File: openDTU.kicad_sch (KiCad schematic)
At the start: 3 parts, among them U1 ESP32NodeMCU, U2 NRF24L01+PA+LNA_Breakout

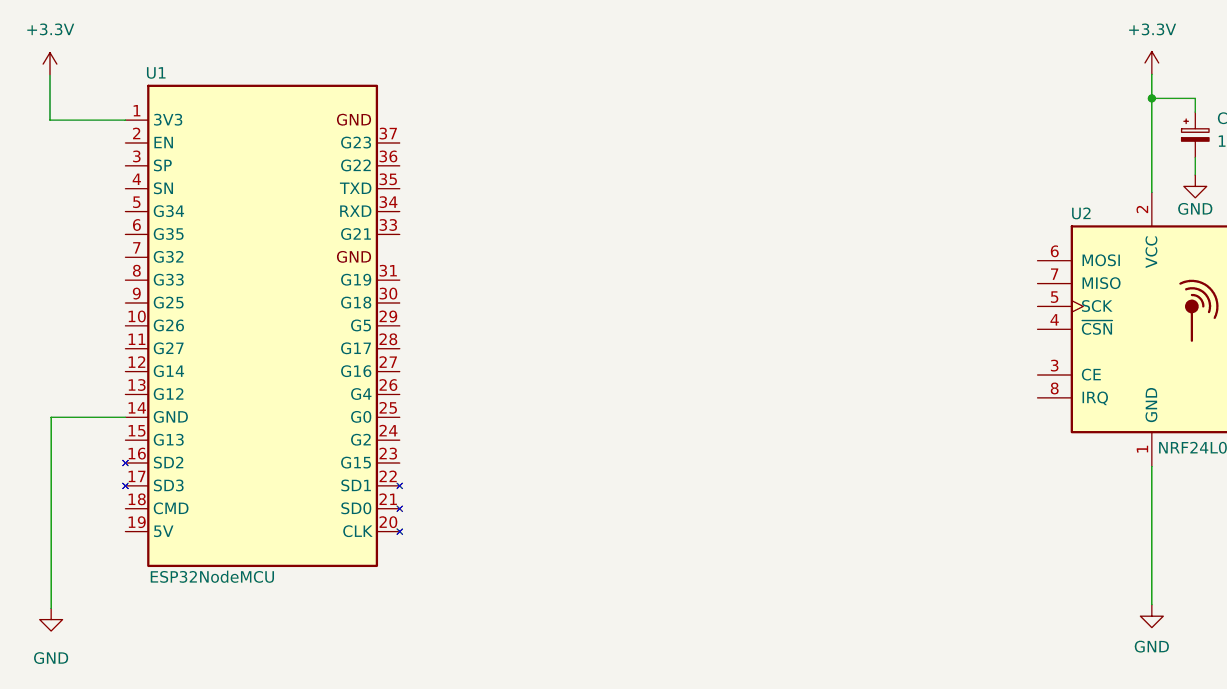
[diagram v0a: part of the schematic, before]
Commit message: connecting nRF24L01+ to the ESP32 in schematic
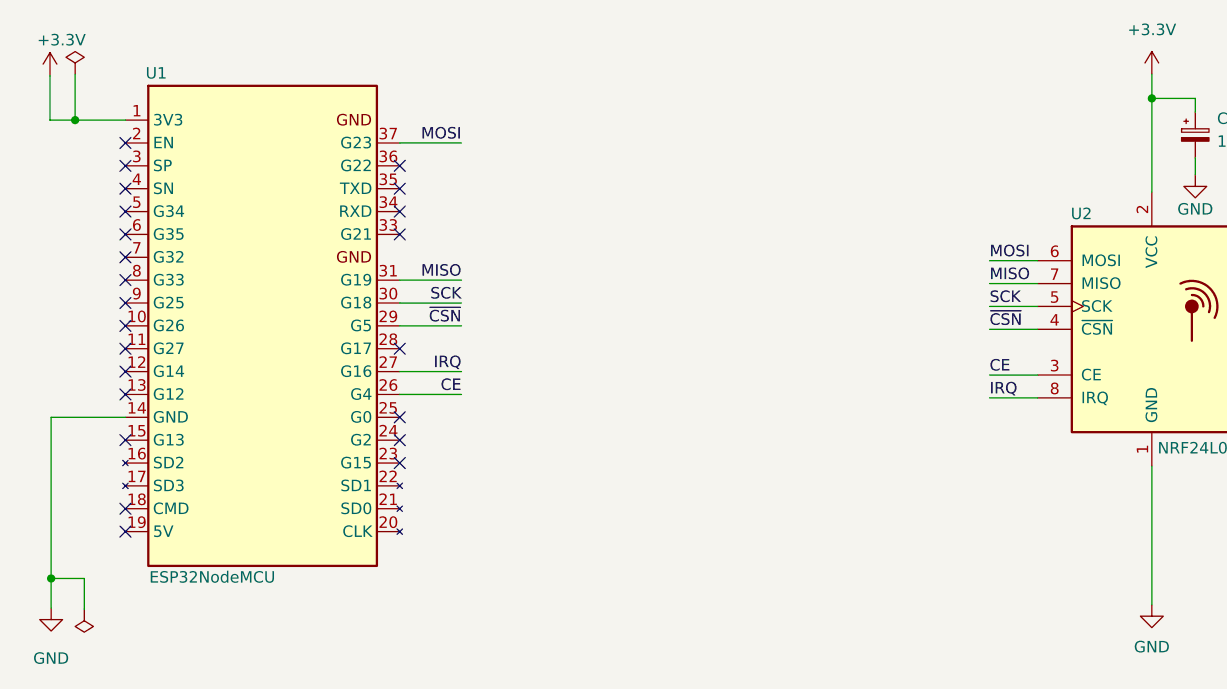
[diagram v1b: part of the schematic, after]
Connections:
- net CE: now reaches U1.26 (G4)
- net CE: now also U2.3 (CE)
- net IRQ: now reaches U1.27 (G16)
- net IRQ: now also U2.8 (IRQ)
- net ~{CSN}: now reaches U1.29 (G5)
- net ~{CSN}: now also U2.4 (~{CSN})
- net SCK: now reaches U1.30 (G18)
- net SCK: now also U2.5 (SCK)
- net MISO: now reaches U1.31 (G19)
- net MISO: now also U2.7 (MISO)
- net MOSI: now reaches U1.37 (G23)
- net MOSI: now also U2.6 (MOSI)
- no-connect marks 0 -> 23
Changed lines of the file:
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@@
 (kicad_sch (version 20211123) (generator eeschema)
   (paper "A4")
+  (junction (at 81.407 77.343) (diameter 0) (color 0 0 0 0)
+  )
   (junction (at 201.041 74.93) (diameter 0) (color 0 0 0 0)
   )
+  (junction (at 78.74 128.27) (diameter 0) (color 0 0 0 0)
+  )
+  (no_connect (at 86.995 123.063))
+  (no_connect (at 86.995 120.523))
+  (no_connect (at 86.995 107.823))
+  (no_connect (at 86.995 79.883))
+  (no_connect (at 86.995 92.583))
+  (no_connect (at 86.995 90.043))
+  (no_connect (at 86.995 87.503))
+  (no_connect (at 86.995 84.963))
+  (no_connect (at 86.995 82.423))
+  (no_connect (at 117.475 90.043))
+  (no_connect (at 117.475 84.963))
+  (no_connect (at 117.475 87.503))
+  (no_connect (at 117.475 82.423))
+  (no_connect (at 117.475 102.743))
+  (no_connect (at 117.475 110.363))
+  (no_connect (at 117.475 112.903))
+  (no_connect (at 117.475 115.443))
+  (no_connect (at 86.995 112.903))
+  (no_connect (at 86.995 105.283))
+  (no_connect (at 86.995 102.743))
+  (no_connect (at 86.995 100.203))
+  (no_connect (at 86.995 97.663))
+  (no_connect (at 86.995 95.123))
+  (wire (pts (xy 117.475 79.883) (xy 124.333 79.883))
+    (stroke (width 0) (type default) (color 0 0 0 0))
+  )
+  (wire (pts (xy 117.475 105.283) (xy 124.333 105.283))
+    (stroke (width 0) (type default) (color 0 0 0 0))
+  )
   (wire (pts (xy 205.867 74.93) (xy 201.041 74.93))
     (stroke (width 0) (type default) (color 0 0 0 0))
   )
+  (wire (pts (xy 183.007 100.584) (xy 188.341 100.584))
+    (stroke (width 0) (type default) (color 0 0 0 0))
+  )
+  (wire (pts (xy 117.475 97.663) (xy 124.333 97.663))
+    (stroke (width 0) (type default) (color 0 0 0 0))
+  )
   (wire (pts (xy 78.74 110.363) (xy 86.995 110.363))
     (stroke (width 0) (type default) (color 0 0 0 0))
   )
-  (wire (pts (xy 78.74 131.572) (xy 78.74 110.363))
+  (wire (pts (xy 78.74 131.572) (xy 78.74 128.27))
+    (stroke (width 0) (type default) (color 0 0 0 0))
+  )
+  (wire (pts (xy 117.475 95.123) (xy 124.333 95.123))
+    (stroke (width 0) (type default) (color 0 0 0 0))
+  )
+  (wire (pts (xy 78.74 128.27) (xy 78.74 110.363))
     (stroke (width 0) (type default) (color 0 0 0 0))
   )
@@
     (stroke (width 0) (type default) (color 0 0 0 0))
   )
+  (wire (pts (xy 183.007 98.044) (xy 188.341 98.044))
+    (stroke (width 0) (type default) (color 0 0 0 0))
+  )
+  (wire (pts (xy 117.475 107.823) (xy 124.333 107.823))
+    (stroke (width 0) (type default) (color 0 0 0 0))
+  )
+  (wire (pts (xy 183.007 108.204) (xy 188.341 108.204))
+    (stroke (width 0) (type default) (color 0 0 0 0))
+  )
   (wire (pts (xy 205.867 81.534) (xy 205.867 83.439))
     (stroke (width 0) (type default) (color 0 0 0 0))
@@
     (stroke (width 0) (type default) (color 0 0 0 0))
   )
+  (wire (pts (xy 183.007 95.504) (xy 188.341 95.504))
+    (stroke (width 0) (type default) (color 0 0 0 0))
+  )
+  (wire (pts (xy 183.007 105.664) (xy 188.341 105.664))
+    (stroke (width 0) (type default) (color 0 0 0 0))
+  )
+  (wire (pts (xy 117.475 100.203) (xy 124.333 100.203))
+    (stroke (width 0) (type default) (color 0 0 0 0))
+  )
+  (wire (pts (xy 81.407 77.343) (xy 86.995 77.343))
+    (stroke (width 0) (type default) (color 0 0 0 0))
+  )
   (wire (pts (xy 201.041 85.344) (xy 201.041 74.93))
     (stroke (width 0) (type default) (color 0 0 0 0))
   )
+  (wire (pts (xy 81.407 72.263) (xy 81.407 77.343))
+    (stroke (width 0) (type default) (color 0 0 0 0))
+  )
   (wire (pts (xy 201.041 74.93) (xy 201.041 72.263))
     (stroke (width 0) (type default) (color 0 0 0 0))
   )
-  (wire (pts (xy 78.613 77.343) (xy 86.995 77.343))
-    (stroke (width 0) (type default) (color 0 0 0 0))
+  (wire (pts (xy 82.423 128.27) (xy 78.74 128.27))
+    (stroke (width 0) (type default) (color 0 0 0 0))
+  )
+  (wire (pts (xy 183.007 92.964) (xy 188.341 92.964))
+    (stroke (width 0) (type default) (color 0 0 0 0))
+  )
+  (wire (pts (xy 78.613 77.343) (xy 81.407 77.343))
+    (stroke (width 0) (type default) (color 0 0 0 0))
+  )
+  (wire (pts (xy 82.423 131.699) (xy 82.423 128.27))
+    (stroke (width 0) (type default) (color 0 0 0 0))
+  )
+  (label "CE" (at 124.333 107.823 180)
+    (effects (font (size 1.27 1.27)) (justify right bottom))
+  )
+  (label "IRQ" (at 124.333 105.283 180)
+    (effects (font (size 1.27 1.27)) (justify right bottom))
+  )
+  (label "~{CSN}" (at 124.333 100.203 180)
+    (effects (font (size 1.27 1.27)) (justify right bottom))
+  )
+  (label "MISO" (at 124.333 95.123 180)
+    (effects (font (size 1.27 1.27)) (justify right bottom))
+  )
+  (label "SCK" (at 183.007 98.044 0)
+    (effects (font (size 1.27 1.27)) (justify left bottom))
+  )
+  (label "MOSI" (at 183.007 92.964 0)
+    (effects (font (size 1.27 1.27)) (justify left bottom))
+  )
+  (label "~{CSN}" (at 183.007 100.584 0)
+    (effects (font (size 1.27 1.27)) (justify left bottom))
+  )
+  (label "MOSI" (at 124.333 79.883 180)
+    (effects (font (size 1.27 1.27)) (justify right bottom))
+  )
+  (label "MISO" (at 183.007 95.504 0)
+    (effects (font (size 1.27 1.27)) (justify left bottom))
+  )
+  (label "CE" (at 183.007 105.664 0)
+    (effects (font (size 1.27 1.27)) (justify left bottom))
+  )
+  (label "IRQ" (at 183.007 108.204 0)
+    (effects (font (size 1.27 1.27)) (justify left bottom))
+  )
+  (label "SCK" (at 124.333 97.663 180)
+    (effects (font (size 1.27 1.27)) (justify right bottom))
   )
   (symbol (lib_id "ESP32-NodeMCU_WROOM_32:ESP32NodeMCU") (at 100.965 100.203 0) (unit 1)
@@
     (pin "2")
   )
+  (symbol (lib_id "power:PWR_FLAG") (at 81.407 72.263 0) (unit 1)
+    (in_bom yes) (on_board yes)
+    (property "Reference" "#FLG0101" (id 0) (at 81.407 70.358 0)
+      (effects (font (size 1.27 1.27)) hide)
+    )
+    (property "Value" "PWR_FLAG" (id 1) (at 81.407 67.31 0)
+      (effects (font (size 1.27 1.27)) hide)
+    )
+    (property "Footprint" "" (id 2) (at 81.407 72.263 0)
+      (effects (font (size 1.27 1.27)) hide)
+    )
+    (property "Datasheet" "~" (id 3) (at 81.407 72.263 0)
+      (effects (font (size 1.27 1.27)) hide)
+    )
+    (pin "1")
+  )
   (symbol (lib_id "nRF24L01+PA+LNA:NRF24L01+PA+LNA_Breakout") (at 201.041 100.584 0) (unit 1)
     (in_bom yes) (on_board yes)
@@
   )
   (symbol (lib_id "power:+3.3V") (at 78.613 72.39 0) (unit 1)
-    (in_bom yes) (on_board yes) (fields_autoplaced)
+    (in_bom yes) (on_board yes)
     (property "Reference" "#PWR01" (id 0) (at 78.613 76.2 0)
       (effects (font (size 1.27 1.27)) hide)
     )
-    (property "Value" "+3.3V" (id 1) (at 78.613 67.31 0))
+    (property "Value" "+3.3V" (id 1) (at 79.883 68.453 0))
     (property "Footprint" "" (id 2) (at 78.613 72.39 0)
       (effects (font (size 1.27 1.27)) hide)
@@
     (pin "1")
   )
+  (symbol (lib_id "power:PWR_FLAG") (at 82.423 131.699 180) (unit 1)
+    (in_bom yes) (on_board yes) (fields_autoplaced)
+    (property "Reference" "#FLG0102" (id 0) (at 82.423 133.604 0)
+      (effects (font (size 1.27 1.27)) hide)
+    )
+    (property "Value" "PWR_FLAG" (id 1) (at 82.423 137.16 0)
+      (effects (font (size 1.27 1.27)) hide)
+    )
+    (property "Footprint" "" (id 2) (at 82.423 131.699 0)
+      (effects (font (size 1.27 1.27)) hide)
+    )
+    (property "Datasheet" "~" (id 3) (at 82.423 131.699 0)
+      (effects (font (size 1.27 1.27)) hide)
+    )
+    (pin "1")
+  )
   (symbol (lib_id "power:GND") (at 205.867 83.439 0) (unit 1)
     (in_bom yes) (on_board yes)
@@
   )
   (symbol_instances
+    (path "/536b3283-000a-432e-99b7-ba775fb60222"
+      (reference "#FLG0101") (unit 1) (value "PWR_FLAG") (footprint "")
+    )
+    (path "/ef63471f-d6f9-4ef1-a573-5457f22963dc"
+      (reference "#FLG0102") (unit 1) (value "PWR_FLAG") (footprint "")
+    )
     (path "/cd7881ec-7c4b-4a13-beb3-1ca57ea56ce1"
       (reference "#PWR01") (unit 1) (value "+3.3V") (footprint "")

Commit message: adding OpenDTU Logo and some informations on the silkscreen
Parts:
- C1: footprint Capacitor_THT:CP_Radial_D6.3mm_P2.50mm -> Capacitor_THT:CP_Radial_D5.0mm_P2.50mm; Manf (none) -> https://www.reichelt.de/de/de/elko-radial-10-f-25-v-105-4-x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
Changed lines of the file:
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@@
       (effects (font (size 1.27 1.27)) (justify left))
     )
-    (property "Footprint" "Capacitor_THT:CP_Radial_D6.3mm_P2.50mm" (id 2) (at 205.867 78.994 0)
+    (property "Footprint" "Capacitor_THT:CP_Radial_D5.0mm_P2.50mm" (id 2) (at 205.867 78.994 0)
       (effects (font (size 1.27 1.27)) hide)
     )
     (property "Datasheet" "~" (id 3) (at 205.867 78.994 0)
+      (effects (font (size 1.27 1.27)) hide)
+    )
+    (property "Manf" "https://www.reichelt.de/de/de/elko-radial-10-f-25-v-105-4-x-7-mm-rm-2-5-ga-a-10u-25-3-p228366.html?r=1" (id 4) (at 205.867 78.994 0)
       (effects (font (size 1.27 1.27)) hide)
     )
@@
     )
     (path "/45a05041-9552-4705-9a03-84bdba86756f"
-      (reference "C1") (unit 1) (value "10uF") (footprint "Capacitor_THT:CP_Radial_D6.3mm_P2.50mm")
+      (reference "C1") (unit 1) (value "10uF") (footprint "Capacitor_THT:CP_Radial_D5.0mm_P2.50mm")
     )
     (path "/0626e94d-7e2b-4dab-a267-2ede4e5d9e77"

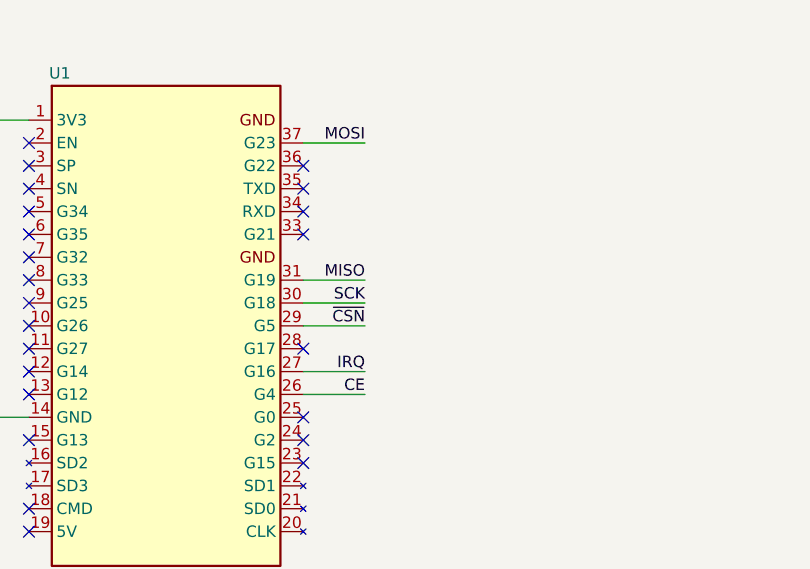
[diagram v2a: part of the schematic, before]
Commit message: Adding some Testpads for signals between ESP32 and nRF24L01+. Adding vias to connect Bottom and Top GND Copper Zone.
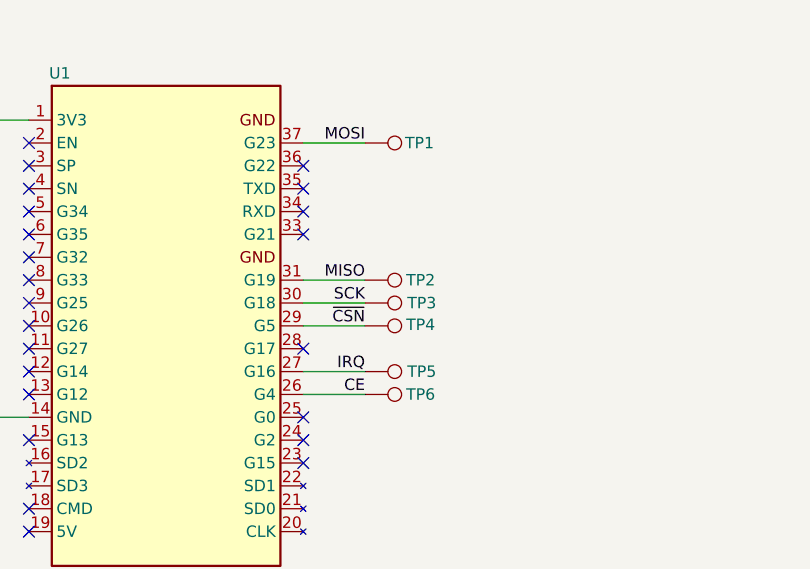
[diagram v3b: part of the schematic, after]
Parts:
- added TP1, TP2, TP3, TP4, TP5, TP6: TestPoint, TestPoint:TestPoint_THTPad_D1.5mm_Drill0.7mm, symbol Connector:TestPoint
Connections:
- net CE: now also TP6.1
- net IRQ: now also TP5.1
- net MISO: now also TP2.1
- net MOSI: now also TP1.1
- net SCK: now also TP3.1
- net ~{CSN}: now also TP4.1
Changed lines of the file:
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@@
     (pin "9")
+  )
+  (symbol (lib_id "Connector:TestPoint") (at 124.333 95.123 270) (unit 1)
+    (in_bom yes) (on_board yes)
+    (property "Reference" "TP2" (id 0) (at 128.905 95.123 90)
+      (effects (font (size 1.27 1.27)) (justify left))
+    )
+    (property "Value" "TestPoint" (id 1) (at 129.54 96.3929 90)
+      (effects (font (size 1.27 1.27)) (justify left) hide)
+    )
+    (property "Footprint" "TestPoint:TestPoint_THTPad_D1.5mm_Drill0.7mm" (id 2) (at 124.333 100.203 0)
+      (effects (font (size 1.27 1.27)) hide)
+    )
+    (property "Datasheet" "~" (id 3) (at 124.333 100.203 0)
+      (effects (font (size 1.27 1.27)) hide)
+    )
+    (pin "1")
   )
   (symbol (lib_id "power:GND") (at 201.041 131.191 0) (unit 1)
@@
     )
     (property "Datasheet" "~" (id 3) (at 81.407 72.263 0)
+      (effects (font (size 1.27 1.27)) hide)
+    )
+    (pin "1")
+  )
+  (symbol (lib_id "Connector:TestPoint") (at 124.333 107.823 270) (unit 1)
+    (in_bom yes) (on_board yes)
+    (property "Reference" "TP6" (id 0) (at 128.905 107.823 90)
+      (effects (font (size 1.27 1.27)) (justify left))
+    )
+    (property "Value" "TestPoint" (id 1) (at 129.54 109.0929 90)
+      (effects (font (size 1.27 1.27)) (justify left) hide)
+    )
+    (property "Footprint" "TestPoint:TestPoint_THTPad_D1.5mm_Drill0.7mm" (id 2) (at 124.333 112.903 0)
+      (effects (font (size 1.27 1.27)) hide)
+    )
+    (property "Datasheet" "~" (id 3) (at 124.333 112.903 0)
+      (effects (font (size 1.27 1.27)) hide)
+    )
+    (pin "1")
+  )
+  (symbol (lib_id "Connector:TestPoint") (at 124.333 97.663 270) (unit 1)
+    (in_bom yes) (on_board yes)
+    (property "Reference" "TP3" (id 0) (at 129.032 97.663 90)
+      (effects (font (size 1.27 1.27)) (justify left))
+    )
+    (property "Value" "TestPoint" (id 1) (at 129.54 98.9329 90)
+      (effects (font (size 1.27 1.27)) (justify left) hide)
+    )
+    (property "Footprint" "TestPoint:TestPoint_THTPad_D1.5mm_Drill0.7mm" (id 2) (at 124.333 102.743 0)
+      (effects (font (size 1.27 1.27)) hide)
+    )
+    (property "Datasheet" "~" (id 3) (at 124.333 102.743 0)
       (effects (font (size 1.27 1.27)) hide)
     )
@@
     (pin "8")
   )
+  (symbol (lib_id "Connector:TestPoint") (at 124.333 79.883 270) (unit 1)
+    (in_bom yes) (on_board yes)
+    (property "Reference" "TP1" (id 0) (at 128.778 79.883 90)
+      (effects (font (size 1.27 1.27)) (justify left))
+    )
+    (property "Value" "TestPoint" (id 1) (at 129.54 81.1529 90)
+      (effects (font (size 1.27 1.27)) (justify left) hide)
+    )
+    (property "Footprint" "TestPoint:TestPoint_THTPad_D1.5mm_Drill0.7mm" (id 2) (at 124.333 84.963 0)
+      (effects (font (size 1.27 1.27)) hide)
+    )
+    (property "Datasheet" "~" (id 3) (at 124.333 84.963 0)
+      (effects (font (size 1.27 1.27)) hide)
+    )
+    (pin "1")
+  )
   (symbol (lib_id "power:+3.3V") (at 78.613 72.39 0) (unit 1)
     (in_bom yes) (on_board yes)
@@
     )
     (property "Datasheet" "" (id 3) (at 201.041 72.263 0)
+      (effects (font (size 1.27 1.27)) hide)
+    )
+    (pin "1")
+  )
+  (symbol (lib_id "Connector:TestPoint") (at 124.333 105.283 270) (unit 1)
+    (in_bom yes) (on_board yes)
+    (property "Reference" "TP5" (id 0) (at 129.032 105.283 90)
+      (effects (font (size 1.27 1.27)) (justify left))
+    )
+    (property "Value" "TestPoint" (id 1) (at 129.54 106.5529 90)
+      (effects (font (size 1.27 1.27)) (justify left) hide)
+    )
+    (property "Footprint" "TestPoint:TestPoint_THTPad_D1.5mm_Drill0.7mm" (id 2) (at 124.333 110.363 0)
+      (effects (font (size 1.27 1.27)) hide)
+    )
+    (property "Datasheet" "~" (id 3) (at 124.333 110.363 0)
+      (effects (font (size 1.27 1.27)) hide)
+    )
+    (pin "1")
+  )
+  (symbol (lib_id "Connector:TestPoint") (at 124.333 100.203 270) (unit 1)
+    (in_bom yes) (on_board yes)
+    (property "Reference" "TP4" (id 0) (at 128.905 100.076 90)
+      (effects (font (size 1.27 1.27)) (justify left))
+    )
+    (property "Value" "TestPoint" (id 1) (at 129.54 101.4729 90)
+      (effects (font (size 1.27 1.27)) (justify left) hide)
+    )
+    (property "Footprint" "TestPoint:TestPoint_THTPad_D1.5mm_Drill0.7mm" (id 2) (at 124.333 105.283 0)
+      (effects (font (size 1.27 1.27)) hide)
+    )
+    (property "Datasheet" "~" (id 3) (at 124.333 105.283 0)
       (effects (font (size 1.27 1.27)) hide)
     )
@@
       (reference "C1") (unit 1) (value "10uF") (footprint "Capacitor_THT:CP_Radial_D5.0mm_P2.50mm")
     )
+    (path "/9271389f-8f34-47d5-a739-8e5c6be39255"
+      (reference "TP1") (unit 1) (value "TestPoint") (footprint "TestPoint:TestPoint_THTPad_D1.5mm_Drill0.7mm")
+    )
+    (path "/138fc2e0-841b-4c13-b27f-6bb74058adc3"
+      (reference "TP2") (unit 1) (value "TestPoint") (footprint "TestPoint:TestPoint_THTPad_D1.5mm_Drill0.7mm")
+    )
+    (path "/6b673ecf-c15b-4bd0-a3f7-7e07b3cef490"
+      (reference "TP3") (unit 1) (value "TestPoint") (footprint "TestPoint:TestPoint_THTPad_D1.5mm_Drill0.7mm")
+    )
+    (path "/ea569931-937f-449b-8d4f-5ad135e4e84a"
+      (reference "TP4") (unit 1) (value "TestPoint") (footprint "TestPoint:TestPoint_THTPad_D1.5mm_Drill0.7mm")
+    )
+    (path "/e569dd78-d048-4b76-ae41-53d4cb054556"
+      (reference "TP5") (unit 1) (value "TestPoint") (footprint "TestPoint:TestPoint_THTPad_D1.5mm_Drill0.7mm")
+    )
+    (path "/6487eed5-4bbb-4c7c-a0e2-f2db5ce1a843"
+      (reference "TP6") (unit 1) (value "TestPoint") (footprint "TestPoint:TestPoint_THTPad_D1.5mm_Drill0.7mm")
+    )
     (path "/0626e94d-7e2b-4dab-a267-2ede4e5d9e77"
